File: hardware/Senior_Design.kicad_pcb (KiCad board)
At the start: 4 copper layers, 169 x 146 mm, 155 parts, among them J1 J0011D21BNL, J20 USB_C_Receptacle_USB2.0_16P, J22 Conn_ARM_JTAG_SWD_10, J5 Conn_ARM_JTAG_SWD_10, J6 Barrel_Jack_Switch, Q3 CSD87503Q3E, Q4 CSD87503Q3E, SW1 SW_Push, SW3 SW_Push, U1 USBLC6-2P6, U10 TLV62569ADRL, U2 EFR32FG28A122F1024GM48-A, U20 USBLC6-2P6, U21 USBLC6-2P6, U22 W5500, U23 BDE-MB1352P71UA32, U3 USBLC6-2P6, U33 USBLC6-2P6, U4 TPS61022, U5 BQ25798RQMR, U59 USBLC6-2P6, U6 BME688, U7 USBLC6-2P6, U8 CP2102N-A02-GQFN20, U9 USBLC6-2P6, X1 Crystal_GND2, Y65 25MHz

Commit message: footprint update
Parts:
- added C202: 1uF, Capacitor_SMD:C_0805_2012Metric, F.Cu at (81.9, -146.0)
- added C203: 2.7uF, Capacitor_SMD:C_0805_2012Metric, F.Cu at (81.9, -143.0)
- added C204: 1uF, Capacitor_SMD:C_0805_2012Metric, F.Cu at (81.9, -140.0)
- added C205: 1uF, Capacitor_SMD:C_0805_2012Metric, F.Cu at (81.9, -137.0)
- added C206: 10nF, Capacitor_SMD:C_0805_2012Metric, F.Cu at (81.9, -133.9)
- added C207: 0.1uF, Capacitor_SMD:C_0805_2012Metric, F.Cu at (81.9, -130.9)
- added C208: 0.1uF, Capacitor_SMD:C_0805_2012Metric, F.Cu at (81.9, -127.9)
- added C209: 0.1uF, Capacitor_SMD:C_0805_2012Metric, F.Cu at (81.9, -124.9)
- added C304: 10uF, Capacitor_SMD:C_0805_2012Metric, F.Cu at (60.8, -146.0)
- added C305: 10uF, Capacitor_SMD:C_0805_2012Metric, F.Cu at (60.8, -143.0)
- added C306: 100nF, Capacitor_SMD:C_0805_2012Metric, F.Cu at (60.8, -140.0)
- added C312: 22uF, Capacitor_SMD:C_0805_2012Metric, F.Cu at (60.8, -137.0)
- added C313: 22uF, Capacitor_SMD:C_0805_2012Metric, F.Cu at (60.8, -133.9)
- added C314: 22uF, Capacitor_SMD:C_0805_2012Metric, F.Cu at (60.8, -130.9)
- added C316: 10uF, Capacitor_SMD:C_0805_2012Metric, F.Cu at (60.8, -127.9)
- added C329: 10uF, Capacitor_SMD:C_0805_2012Metric, F.Cu at (60.8, -124.9)
- added D202: LED, LED_SMD:LED_0805_2012Metric, F.Cu at (90.8, -146.0)
- added D203: LED, LED_SMD:LED_0805_2012Metric, F.Cu at (90.8, -142.9)
- added D204: LED, LED_SMD:LED_0805_2012Metric, F.Cu at (90.8, -139.9)
- added D601: LED, LED_SMD:LED_0805_2012Metric, F.Cu at (60.8, -114.9)
- added D602: LED, LED_SMD:LED_0805_2012Metric, F.Cu at (60.8, -111.9)
- added IC301: TLV61220DBVT, pyronet_footprints:SOT95P280X110-6, F.Cu at (75.3, -145.0)
- added J302: Conn_01x03, Connector_JST:JST_PH_S3B-PH-K_1x03_P2.00mm_Horizontal, F.Cu at (66.0, -145.1)
- added L301: 1.5uH, Inductor_SMD:L_0805_2012Metric, F.Cu at (75.1, -136.5)
- added L303: 4.7uH, Inductor_SMD:L_0805_2012Metric, F.Cu at (75.1, -133.7)
- added Q303: Q_NMOS, Package_TO_SOT_SMD:SOT-23_Handsoldering, F.Cu at (71.7, -128.0)
- added R202: 4.7k, Resistor_SMD:R_0805_2012Metric, F.Cu at (86.3, -146.0)
- added R203: 4.7k, Resistor_SMD:R_0805_2012Metric, F.Cu at (86.3, -143.1)
- added R204: 220, Resistor_SMD:R_0805_2012Metric, F.Cu at (86.3, -140.1)
- added R205: 220, Resistor_SMD:R_0805_2012Metric, F.Cu at (86.3, -137.2)
- added R206: 220, Resistor_SMD:R_0805_2012Metric, F.Cu at (86.3, -134.2)
- added R304: 1M, Resistor_SMD:R_0805_2012Metric, F.Cu at (65.2, -136.4)
- added R305: 180k, Resistor_SMD:R_0805_2012Metric, F.Cu at (65.2, -133.4)
- added R308: 1M, Resistor_SMD:R_0805_2012Metric, F.Cu at (65.2, -130.5)
- added R312: 909K, Resistor_SMD:R_0805_2012Metric, F.Cu at (65.2, -127.5)
- added R313: 100K, Resistor_SMD:R_0805_2012Metric, F.Cu at (65.2, -124.6)
- added R402: 10k, Resistor_SMD:R_0805_2012Metric, F.Cu at (71.6, -119.6)
- added R606: 220, Resistor_SMD:R_0805_2012Metric, F.Cu at (65.2, -115.0)
- added R607: 220, Resistor_SMD:R_0805_2012Metric, F.Cu at (65.2, -112.0)
- added U301: TPS63020DSJR, pyronet_footprints:IC_TPS63020DSJR, F.Cu at (70.3, -134.9)
- added U602: CDSOT236-0504C, Package_TO_SOT_SMD:SOT-23-6, F.Cu at (61.1, -118.7)
- added U701: W5500, Package_QFP:LQFP-48_7x7mm_P0.5mm, F.Cu at (85.3, -115.7)
- added Y201: LF_Crystal, Crystal:Crystal_SMD_3215-2Pin_3.2x1.5mm, F.Cu at (86.6, -131.1)
- C201: renamed from C19; footprint Capacitor_SMD:C_0402_1005Metric -> Capacitor_SMD:C_0805_2012Metric
- C301: renamed from C40; footprint Capacitor_SMD:C_0402_1005Metric -> Capacitor_SMD:C_0805_2012Metric
- C302: renamed from C44; footprint Capacitor_SMD:C_0402_1005Metric -> Capacitor_SMD:C_0805_2012Metric
- C303: renamed from C45; footprint Capacitor_SMD:C_0402_1005Metric -> Capacitor_SMD:C_0805_2012Metric
- C307: renamed from C46; footprint Capacitor_SMD:C_0402_1005Metric -> Capacitor_SMD:C_0805_2012Metric
- C308: renamed from C47; footprint Capacitor_SMD:C_0402_1005Metric -> Capacitor_SMD:C_0805_2012Metric
- C309: renamed from C49; footprint Capacitor_SMD:C_0402_1005Metric -> Capacitor_SMD:C_0805_2012Metric
- C310: renamed from C50; footprint Capacitor_SMD:C_0402_1005Metric -> Capacitor_SMD:C_0805_2012Metric
- C311: renamed from C51; footprint Capacitor_SMD:C_0402_1005Metric -> Capacitor_SMD:C_0805_2012Metric
- C315: renamed from C55; footprint Capacitor_SMD:C_0402_1005Metric -> Capacitor_SMD:C_0805_2012Metric
- C317: renamed from C67; footprint Capacitor_SMD:C_0402_1005Metric -> Capacitor_SMD:C_0805_2012Metric
- C318: renamed from C69; footprint Capacitor_SMD:C_0402_1005Metric -> Capacitor_SMD:C_0805_2012Metric
- C319: renamed from C52; footprint Capacitor_SMD:C_0402_1005Metric -> Capacitor_SMD:C_0805_2012Metric
- C320: renamed from C68; footprint Capacitor_SMD:C_0402_1005Metric -> Capacitor_SMD:C_0805_2012Metric
- C321: renamed from C71; footprint Capacitor_SMD:C_0402_1005Metric -> Capacitor_SMD:C_0805_2012Metric
- C322: renamed from C53; footprint Capacitor_SMD:C_0402_1005Metric -> Capacitor_SMD:C_0805_2012Metric
- C323: renamed from C70; footprint Capacitor_SMD:C_0402_1005Metric -> Capacitor_SMD:C_0805_2012Metric
- C324: renamed from C73; footprint Capacitor_SMD:C_0402_1005Metric -> Capacitor_SMD:C_0805_2012Metric
- C325: renamed from C54; footprint Capacitor_SMD:C_0402_1005Metric -> Capacitor_SMD:C_0805_2012Metric
- C326: renamed from C72; footprint Capacitor_SMD:C_0402_1005Metric -> Capacitor_SMD:C_0805_2012Metric
- C327: renamed from C75; footprint Capacitor_SMD:C_0402_1005Metric -> Capacitor_SMD:C_0805_2012Metric
- C328: renamed from C74; footprint Capacitor_SMD:C_0402_1005Metric -> Capacitor_SMD:C_0805_2012Metric
- C401: renamed from C1; footprint Capacitor_SMD:C_0603_1608Metric -> Capacitor_SMD:C_0805_2012Metric
- C402: renamed from C10; footprint Capacitor_SMD:C_0402_1005Metric -> Capacitor_SMD:C_0805_2012Metric
- C403: renamed from C2; footprint Capacitor_SMD:C_0402_1005Metric -> Capacitor_SMD:C_0805_2012Metric
- C501: renamed from C25; footprint Capacitor_SMD:C_0402_1005Metric -> Capacitor_SMD:C_0805_2012Metric
- C502: renamed from C12; footprint Capacitor_SMD:C_0402_1005Metric -> Capacitor_SMD:C_0805_2012Metric
- C601: renamed from C90; footprint Capacitor_SMD:C_0402_1005Metric -> Capacitor_SMD:C_0805_2012Metric
- C602: renamed from C14; footprint Capacitor_SMD:C_0402_1005Metric -> Capacitor_SMD:C_0805_2012Metric
- C701: renamed from C7; footprint Capacitor_SMD:C_0402_1005Metric -> Capacitor_SMD:C_0805_2012Metric
- C702: renamed from C9; footprint Capacitor_SMD:C_0402_1005Metric -> Capacitor_SMD:C_0805_2012Metric
- C703: renamed from C8; footprint Capacitor_SMD:C_0402_1005Metric -> Capacitor_SMD:C_0805_2012Metric
- C704: renamed from C27; footprint Capacitor_SMD:C_0402_1005Metric -> Capacitor_SMD:C_0805_2012Metric
- C705: renamed from C100; footprint Capacitor_SMD:C_0402_1005Metric -> Capacitor_SMD:C_0805_2012Metric
- C706: renamed from C56; footprint Capacitor_SMD:C_0402_1005Metric -> Capacitor_SMD:C_0805_2012Metric
- C707: renamed from C28; footprint Capacitor_SMD:C_0402_1005Metric -> Capacitor_SMD:C_0805_2012Metric
- C708: renamed from C3; footprint Capacitor_SMD:C_0402_1005Metric -> Capacitor_SMD:C_0805_2012Metric
- C709: renamed from C29; footprint Capacitor_SMD:C_0402_1005Metric -> Capacitor_SMD:C_0805_2012Metric
- C710: renamed from C4; footprint Capacitor_SMD:C_0402_1005Metric -> Capacitor_SMD:C_0805_2012Metric
- C711: renamed from C5; footprint Capacitor_SMD:C_0402_1005Metric -> Capacitor_SMD:C_0805_2012Metric
- C712: renamed from C39; footprint Capacitor_SMD:C_0402_1005Metric -> Capacitor_SMD:C_0805_2012Metric
- C713: renamed from C82; footprint Capacitor_SMD:C_0402_1005Metric -> Capacitor_SMD:C_0805_2012Metric
- C714: renamed from C34; footprint Capacitor_SMD:C_0402_1005Metric -> Capacitor_SMD:C_0805_2012Metric
- C715: renamed from C38; footprint Capacitor_SMD:C_0402_1005Metric -> Capacitor_SMD:C_0805_2012Metric
- C716: renamed from C41; footprint Capacitor_SMD:C_0402_1005Metric -> Capacitor_SMD:C_0805_2012Metric
- C717: renamed from C42; footprint Capacitor_SMD:C_0402_1005Metric -> Capacitor_SMD:C_0805_2012Metric
- J201: renamed from J5; footprint Connector_PinHeader_1.27mm:PinHeader_2x05_P1.27mm_Vertical -> Connector_PinHeader_1.27mm:PinHeader_2x05_P1.27mm_Vertical_SMD
- J701: renamed from J1; footprint Custom_Parts:CONN_J0011D21B_PUL -> pyronet_footprints:CONN_J0011D21B_PUL
- L302: renamed from L4; footprint Inductor_SMD:L_7.3x7.3_H3.5 -> Inductor_SMD:L_0805_2012Metric
- Q301: renamed from Q3; footprint Custom_Parts:TRANS_CSD87503Q3E -> pyronet_footprints:TRANS_CSD87503Q3ET
- Q302: renamed from Q4; footprint Custom_Parts:TRANS_CSD87503Q3E -> pyronet_footprints:TRANS_CSD87503Q3ET
- R201: renamed from R2; footprint Resistor_SMD:R_0603_1608Metric -> Resistor_SMD:R_0805_2012Metric
- R301: renamed from R10; footprint Resistor_SMD:R_0603_1608Metric -> Resistor_SMD:R_0805_2012Metric
- R302: renamed from R11; footprint Resistor_SMD:R_0603_1608Metric -> Resistor_SMD:R_0805_2012Metric
- R303: renamed from R34; footprint Resistor_SMD:R_0603_1608Metric -> Resistor_SMD:R_0805_2012Metric
- R306: renamed from R_INT1; footprint Resistor_SMD:R_0603_1608Metric -> Resistor_SMD:R_0805_2012Metric
- R307: renamed from R_QON1; footprint Resistor_SMD:R_0603_1608Metric -> Resistor_SMD:R_0805_2012Metric
- R309: renamed from R38; value 100 -> 4.7K; footprint Resistor_SMD:R_0603_1608Metric -> Resistor_SMD:R_0805_2012Metric
- R310: renamed from R39; footprint Resistor_SMD:R_0603_1608Metric -> Resistor_SMD:R_0805_2012Metric
- R311: renamed from R42; footprint Resistor_SMD:R_0603_1608Metric -> Resistor_SMD:R_0805_2012Metric
- R314: renamed from R_TS1; footprint Resistor_SMD:R_0603_1608Metric -> Resistor_SMD:R_0805_2012Metric
- R315: renamed from R_TS3; footprint Resistor_SMD:R_0603_1608Metric -> Resistor_SMD:R_0805_2012Metric
- R401: renamed from R7; value 10k -> 100k; footprint Resistor_SMD:R_0603_1608Metric -> Resistor_SMD:R_0805_2012Metric
- R601: renamed from R14; footprint Resistor_SMD:R_0603_1608Metric -> Resistor_SMD:R_0805_2012Metric
- R602: renamed from R300; footprint Resistor_SMD:R_0603_1608Metric -> Resistor_SMD:R_0805_2012Metric
- R603: renamed from R9; footprint Resistor_SMD:R_0603_1608Metric -> Resistor_SMD:R_0805_2012Metric
- R604: renamed from R27; footprint Resistor_SMD:R_0603_1608Metric -> Resistor_SMD:R_0805_2012Metric
- R605: renamed from R28; footprint Resistor_SMD:R_0603_1608Metric -> Resistor_SMD:R_0805_2012Metric
- R608: renamed from R26; footprint Resistor_SMD:R_0603_1608Metric -> Resistor_SMD:R_0805_2012Metric
- R701: renamed from R80; footprint Resistor_SMD:R_0603_1608Metric -> Resistor_SMD:R_0805_2012Metric
- R702: renamed from R16; footprint Resistor_SMD:R_0603_1608Metric -> Resistor_SMD:R_0805_2012Metric
- R703: renamed from R12; footprint Resistor_SMD:R_0603_1608Metric -> Resistor_SMD:R_0805_2012Metric
- R704: renamed from R13; footprint Resistor_SMD:R_0603_1608Metric -> Resistor_SMD:R_0805_2012Metric
- R705: renamed from R17; footprint Resistor_SMD:R_0603_1608Metric -> Resistor_SMD:R_0805_2012Metric
- R706: renamed from R18; footprint Resistor_SMD:R_0603_1608Metric -> Resistor_SMD:R_0805_2012Metric
- R707: renamed from R1; footprint Resistor_SMD:R_0603_1608Metric -> Resistor_SMD:R_0805_2012Metric
- R708: renamed from R22; footprint Resistor_SMD:R_0603_1608Metric -> Resistor_SMD:R_0805_2012Metric
- R709: renamed from R23; footprint Resistor_SMD:R_0603_1608Metric -> Resistor_SMD:R_0805_2012Metric
- R710: renamed from R19; footprint Resistor_SMD:R_0603_1608Metric -> Resistor_SMD:R_0805_2012Metric
- R711: renamed from R20; footprint Resistor_SMD:R_0603_1608Metric -> Resistor_SMD:R_0805_2012Metric
- R712: renamed from R21; footprint Resistor_SMD:R_0603_1608Metric -> Resistor_SMD:R_0805_2012Metric
- R713: renamed from R15; footprint Resistor_SMD:R_0603_1608Metric -> Resistor_SMD:R_0805_2012Metric
- R714: renamed from R8; footprint Resistor_SMD:R_0603_1608Metric -> Resistor_SMD:R_0805_2012Metric
- U201: renamed from U2; footprint Custom_Parts:QFN40P600X600X90-49N -> pyronet_footprints:QFN40P600X600X90-49N
- U302: renamed from U5; footprint Custom_Parts:IC_BQ25798RQMR -> pyronet_footprints:IC_BQ25798RQMR
- U403: renamed from U23; footprint Custom_Parts:XCVR_BDE-MB1352P71UA32 -> pyronet_footprints:XCVR_BDE-MB1352P71UA32
- U501: renamed from U6; footprint Custom_Parts:IC_BME688 -> pyronet_footprints:IC_BME688
- U603: renamed from U8; footprint Custom_Parts:QFN50P400X400X80-25N -> pyronet_footprints:SILABS_CP2102N-A02-GQFN20R
- X201: renamed from X1; value Crystal_GND2 -> HF_Crystal; footprint Crystal:Crystal_SMD_3225-4Pin_3.2x2.5mm -> Crystal:Crystal_SMD_2016-4Pin_2.0x1.6mm
- moved D4 0.41 mm to (126.0, 23.4)
- renumbered D9 to D201, D10 to D301, D1 to D302, D2 to D303, D5 to D304, D7 to D401, D11 to D501, FB3 to FB701, J6 to J301, J22 to J401, J20 to J601, SPS30_Connector4 to SPS30_Connector501, SW3 to SW201, SW1 to SW401, U20 to U202, U21 to U203, U1 to U401, U3 to U402, U59 to U502, U33 to U601, U7 to U702, U9 to U703, Y65 to Y701
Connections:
- net /Antenna Module/BDE_RESET renamed /MCU/BDE_RESET
- net /Antenna Module/JTAG_TCKC renamed /Wi-SUN Module/JTAG_TCKC
- net /Antenna Module/JTAG_TDI renamed /Wi-SUN Module/JTAG_TDI
- net /Antenna Module/JTAG_TDO renamed /Wi-SUN Module/JTAG_TDO
- net /Antenna Module/JTAG_TMSC renamed /Wi-SUN Module/JTAG_TMSC
- net /Antenna Module/MCU_CTS_BDE_RTS renamed /MCU/MCU_CTS_BDE_RTS
- net /Antenna Module/MCU_RTS_BDE_CTS renamed /MCU/MCU_RTS_BDE_CTS
- net /Antenna Module/MCU_RX_BDE_TX renamed /MCU/MCU_TX_BDE_RX
- net /Antenna Module/MCU_TX_BDE_RX renamed /MCU/MCU_RX_BDE_TX
- net /MCU/28 renamed /MCU/JTAG_TDO
- net /MCU/INT0 renamed /BMS/INT0
- net /PSU/ACDRV1 renamed /BMS/ACDRV1
- net /PSU/ACDRV2 renamed /BMS/ACDRV2
- net /PSU/PMID renamed /BMS/PMID
- net /PSU/REGN renamed /BMS/REGN
- net /PSU/VAC2 renamed /BMS/VAC2
- net /USBC/D_N renamed /USB-C/D_N
- net /USBC/D_P renamed /USB-C/D_P
- net /ethernet/RD+ renamed /Ethernet/RD+
- net /ethernet/RD- renamed /Ethernet/RD-
- net /ethernet/TD+ renamed /Ethernet/TD+
- net /ethernet/TD- renamed /Ethernet/TD-
- net 5V_VBUS renamed USB_VBUS
- net Net-(J20-CC1) renamed /USB-C/CC1
- net Net-(J20-CC2) renamed /USB-C/CC2
- C315 pad 1: /PSU/SYS -> /BMS/SYS
- C317 pad 1: /PSU/SYS -> /BMS/SYS
- C320 pad 1: /PSU/SYS -> /BMS/SYS
- C323 pad 1: /PSU/SYS -> /BMS/SYS
- C326 pad 1: /PSU/SYS -> /BMS/SYS
- C328 pad 1: /PSU/SYS -> /BMS/SYS
- C402 pad 1: BUCK_3.3V -> +3.3V
- C403 pad 1: BUCK_3.3V -> +3.3V
- C601 pad 1: BUCK_3.3V -> +3.3V
- C602 pad 1: BUCK_3.3V -> +3.3V
- C702 pad 1: BUCK_3.3V -> +3.3V
- C703 pad 1: Net-(U22-XO) -> Net-(U701-XO)
- C704 pad 1: BUCK_3.3V -> +3.3V
- C707 pad 1: Net-(U22-1V2O) -> Net-(U701-1V2O)
- C709 pad 1: Net-(U22-TOCAP) -> Net-(U701-TOCAP)
- D201 pad 1: /MCU/JTAG_RST -> /MCU/nRST
- D501 pad 1: BUCK_5V -> +5V
- FB701 pad 1: BUCK_3.3V -> +3.3V
- J201 pad 1: BUCK_3.3V -> +3.3V
- J201 pad 10: /MCU/JTAG_RST -> /MCU/nRST
- J201 pad 2: /MCU/27 -> /MCU/JTAG_TMS
- J201 pad 4: /MCU/26 -> /MCU/JTAG_TCK
- J201 pad 8: unconnected-(J5-NC/TDI-Pad8) -> /MCU/JTAG_TDI
- J401 pad 1: BUCK_3.3V -> +3.3V
- J701 pad 10: Net-(D3-K) -> Net-(J701-Pad10)
- J701 pad 11: BUCK_3.3V -> +3.3V
- J701 pad 12: Net-(D8-K) -> Net-(J701-Pad12)
- J701 pad 9: BUCK_3.3V -> +3.3V
- R306 pad 2: BUCK_3.3V -> +3.3V
- R307 pad 1: /MCU/QON -> /BMS/QON
- R307 pad 2: BUCK_3.3V -> +3.3V
- R311 pad 1: BAT -> Net-(J302-Pin_1)
- R314 pad 1: /PSU/TS -> /BMS/TS
- R315 pad 2: /PSU/TS -> /BMS/TS
- R401 pad 1: BUCK_3.3V -> +3.3V
- R608 pad 1: Net-(U8-RSTB) -> +3.3V
- R608 pad 2: BUCK_3.3V -> Net-(U603-~{RST})
- R701 pad 1: Net-(U22-XI/CLKIN) -> Net-(U701-XI/CLKIN)
- R702 pad 1: Net-(U22-XI/CLKIN) -> Net-(U701-XI/CLKIN)
- R702 pad 2: Net-(U22-XO) -> Net-(U701-XO)
- R703 pad 1: Net-(U22-TXN) -> Net-(U701-TXN)
- R704 pad 1: Net-(U22-TXP) -> Net-(U701-TXP)
- R705 pad 1: Net-(U22-RXN) -> Net-(U701-RXN)
- R706 pad 1: Net-(U22-RXP) -> Net-(U701-RXP)
- R707 pad 1: Net-(U22-EXRES1) -> Net-(U701-EXRES1)
- R713 pad 1: /ethernet/LINKLED -> /Ethernet/LINKLED
- R713 pad 2: Net-(D3-K) -> Net-(J701-Pad10)
- R714 pad 1: /ethernet/ACTLED -> /Ethernet/ACTLED
- R714 pad 2: Net-(D8-K) -> Net-(J701-Pad12)
- SPS30_Connector501 pad 1: BUCK_5V -> +5V
- SW201 pad 2: Net-(U2-~{RESET}) -> /MCU/nRST
- U201 pad 10: /MCU/INT1 -> /Ethernet/INT1
- U201 pad 13: Net-(U2-~{RESET}) -> /MCU/nRST
- U201 pad 14: BUCK_3.3V -> +3.3V
- U201 pad 15: unconnected-(U2-RFVSS-Pad15) -> GND
- U201 pad 20: /MCU/PAVDD -> +3.3V
- U201 pad 26: /MCU/26 -> /MCU/JTAG_TMS
- U201 pad 27: /MCU/27 -> /MCU/JTAG_TCK
- U201 pad 29: unconnected-(U2-PA04-Pad29) -> /MCU/JTAG_TDI
- U201 pad 33: unconnected-(U2-PA08-Pad33) -> /MCU/SPS30_Debug
- U201 pad 34: unconnected-(U2-PA09-Pad34) -> /MCU/BME688_Degbug
- U201 pad 35: /MCU/JTAG_RST -> /MCU/MCU_Debug
- U201 pad 37: /MCU/VREGSW -> unconnected-(U201-VREGSW-Pad37)
- U201 pad 38: BUCK_3.3V -> +3.3V
- U201 pad 39: unconnected-(U2-VREGVSS-Pad39) -> GND
- U201 pad 40: /MCU/DVDD -> +3.3V
- U201 pad 41: BUCK_3.3V -> +3.3V
- U201 pad 42: BUCK_3.3V -> +3.3V
- U201 pad 43: unconnected-(U2-PD05-Pad43) -> /MCU/BDE_DEBUG1
- U201 pad 44: unconnected-(U2-PD04-Pad44) -> /MCU/BDE_DEBUG0
- U201 pad 45: unconnected-(U2-PD03-Pad45) -> /BMS/QON
- U201 pad 46: /Antenna Module/BDE_DEBUG1 -> unconnected-(U201-PD02-Pad46)
- U201 pad 47: /Antenna Module/BDE_DEBUG0 -> Net-(U201-PD01)
- U201 pad 48: /MCU/QON -> Net-(U201-PD00)
- U201 pad 5: /MCU/SPI_MOSI -> /Ethernet/SPI_MOSI
- U201 pad 6: /MCU/SPI_MISO -> /Ethernet/SPI_MISO
- U201 pad 7: /MCU/SPI_SCK -> /Ethernet/SPI_SCK
- U201 pad 8: /MCU/CS -> /Ethernet/CS
- U202 pad 1: /MCU/26 -> /MCU/JTAG_TCK
- U202 pad 3: /MCU/27 -> /MCU/JTAG_TMS
- U202 pad 4: /MCU/27 -> /MCU/JTAG_TMS
- U202 pad 5: BUCK_3.3V -> +3.3V
- U202 pad 6: /MCU/26 -> /MCU/JTAG_TCK
- U203 pad 3: unconnected-(U21-I/O2-Pad3) -> /MCU/JTAG_TDI
- U203 pad 4: unconnected-(U21-I/O2-Pad4) -> /MCU/JTAG_TDI
- U203 pad 5: BUCK_3.3V -> +3.3V
- U302 pad 12: /MCU/QON -> /BMS/QON
- U302 pad 16: /PSU/TS -> /BMS/TS
- U302 pad 24: unconnected-(U5-SDRV-Pad24) -> Net-(U302-SDRV)
- U302 pad 25: /PSU/SYS -> /BMS/SYS
- U401 pad 5: BUCK_3.3V -> +3.3V
- U402 pad 5: BUCK_3.3V -> +3.3V
- U403 pad 16: /Antenna Module/BDE_DEBUG1 -> /MCU/BDE_DEBUG1
- U403 pad 9: /Antenna Module/BDE_DEBUG0 -> /MCU/BDE_DEBUG0
- U501 pad 2: BUCK_3.3V -> +3.3V
- U501 pad 5: GND -> /BME 688 and SPS30/SCL
- U502 pad 5: BUCK_3.3V -> +3.3V
- U603 pad 10: unconnected-(U8-NC-Pad10) -> (no net)
- U603 pad 19: unconnected-(U8-GPIO.3_/_RXT-Pad19) -> Net-(D602-A)
- U603 pad 20: unconnected-(U8-GPIO.2_/_TXT-Pad20) -> Net-(D601-A)
- U603 pad 6: BUCK_3.3V -> +3.3V
- U603 pad 7: BUCK_3.3V -> +3.3V
- U603 pad 9: Net-(U8-RSTB) -> Net-(U603-~{RST})
- U702 pad 5: BUCK_3.3V -> +3.3V
- U703 pad 5: BUCK_3.3V -> +3.3V
- Y701 pad 3: Net-(U22-XO) -> Net-(U701-XO)
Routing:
- net (no net): track 0.00 -> 696.5 mm, vias 0 -> 18
- net USB_VBUS: track 183.8 -> 0.00 mm, vias 6 -> 0
- net Net-(U2-~{RESET}): track 94.3 -> 1.91 mm, vias 2 -> 0
- net /MCU/nRST: track 60.4 -> 152.8 mm, vias 2 -> 4
- net /MCU/JTAG_RST: track 86.3 -> 0.00 mm, vias 1 -> 0
- net /MCU/26: track 79.3 -> 0.00 mm, vias 2 -> 0
- net /MCU/27: track 78.5 -> 0.00 mm, vias 3 -> 0
- net /Antenna Module/BDE_DEBUG0: track 72.6 -> 0.00 mm, vias 2 -> 0
- net /MCU/QON: track 65.2 -> 0.00 mm, vias 2 -> 0
- net /Antenna Module/BDE_DEBUG1: track 57.5 -> 0.00 mm, vias 2 -> 0
- net Net-(C712-Pad1): track 27.2 -> 0.00 mm
- net /Ethernet/TD+: track 24.4 -> 5.22 mm
- net Net-(C714-Pad1): track 9.89 -> 0.00 mm
- net Net-(U603-VBUS): track 5.75 -> 0.00 mm
- net /MCU/JTAG_TMS: track 0.00 -> 4.99 mm, vias 0 -> 1
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- added copper zone on In2.Cu, net +3.3V
- removed copper zone on In2.Cu, net BUCK_3.3V

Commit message: footprint update 2
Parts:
- removed D12, D3, D4, D6, D8: CSD01060A, Package_TO_SOT_THT:TO-220-2_Vertical
- removed J_BAT1: Conn_01x02, Connector_PinHeader_1.27mm:PinHeader_1x02_P1.27mm_Vertical
- removed L2, L7: 1 uH, Inductor_SMD:L_7.3x7.3_H3.5
- removed R40: 453K, Resistor_SMD:R_0603_1608Metric
- removed R41: 100k, Resistor_SMD:R_0603_1608Metric
- removed U10: TLV62569ADRL, Package_TO_SOT_SMD:SOT-563
- removed the U701 at (85.3, -115.7)
- D201, D301, D401, D501: footprint Package_TO_SOT_THT:TO-220-2_Vertical -> Diode_SMD:D_SOD-123
- moved C202 257.9 mm to (-65.3, 65.8)
- moved C203 257.9 mm to (-65.3, 68.8)
- moved C204 257.9 mm to (-65.3, 71.8)
- moved C205 257.9 mm to (-65.3, 74.8)
- moved C206 257.9 mm to (-65.3, 77.8)
- moved C207 257.9 mm to (-65.3, 80.8)
- moved C208 257.9 mm to (-65.3, 83.8)
- moved C209 257.9 mm to (-65.3, 86.8)
- moved C304 257.9 mm to (-86.4, 65.8)
- moved C305 257.9 mm to (-86.4, 68.8)
- moved C306 257.9 mm to (-86.4, 71.8)
- moved C312 257.9 mm to (-86.4, 74.8)
- moved C313 257.9 mm to (-86.4, 77.8)
- moved C314 257.9 mm to (-86.4, 80.8)
- moved C316 257.9 mm to (-86.4, 83.8)
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- renumbered U22 to U701
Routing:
- net /MCU/MCU_Debug: track 0.00 -> 86.3 mm
- net (no net): track 696.5 -> 610.2 mm
- net Net-(J701-Pad12): track 0.00 -> 14.6 mm
- net Net-(D8-K): track 14.6 -> 0.00 mm
- net /MCU/BDE_RESET: track 42.1 -> 32.5 mm
- net Net-(J701-Pad10): track 0.00 -> 5.15 mm
- net Net-(D3-K): track 5.15 -> 0.00 mm

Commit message: layout_246
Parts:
- moved C306 231.4 mm to (129.1, 156.0)
- moved C305 230.0 mm to (128.6, 150.4)
- moved C312 220.5 mm to (122.0, 146.8)
- moved C304 219.5 mm to (120.0, 140.7)
- moved U602 218.6 mm to (123.4, 30.5)
- moved J302 218.5 mm to (130.6, 120.4)
- moved U301 214.1 mm to (128.5, 137.1)
- moved L301 212.8 mm to (129.0, 144.8), turned to 180 degrees
- moved C316 206.8 mm to (106.2, 159.0)
- moved R304 206.4 mm to (108.7, 154.4)
- moved IC301 205.7 mm to (123.2, 132.1)
- moved C313 204.5 mm to (106.2, 146.3)
- moved C314 202.0 mm to (106.2, 141.7)
- moved R305 198.5 mm to (100.7, 156.0)
- moved R313 198.1 mm to (109.8, 136.7)
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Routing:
- net (no net): track 610.2 -> 417.2 mm, vias 18 -> 12
- net USB_VBUS: track 0.00 -> 154.2 mm, vias 0 -> 3
- net /MCU/SPI_MOSI: track 36.9 -> 14.1 mm
- net /Ethernet/SPI_MOSI: track 0.00 -> 22.8 mm
- net /MCU/SPI_MISO: track 35.1 -> 12.9 mm
- net /Ethernet/SPI_MISO: track 0.00 -> 22.2 mm
- net /Ethernet/SPI_SCK: track 0.00 -> 19.0 mm
- net /MCU/SPI_SCK: track 33.5 -> 14.5 mm
- net /Ethernet/CS: track 0.00 -> 18.3 mm
- net /MCU/CS: track 32.0 -> 13.7 mm
- net /MCU/INT1: track 40.5 -> 22.4 mm, vias 4 -> 3
- net /Ethernet/INT1: track 0.00 -> 18.1 mm, vias 0 -> 1
- net /USB-C/D_P: track 12.7 -> 1.54 mm, vias 2 -> 0
- net /USB-C/D_N: track 12.0 -> 2.87 mm
- net Net-(U22-XO): track 14.2 -> 6.94 mm
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
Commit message: pcb_update_1232
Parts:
- removed C16: 10uF, Capacitor_SMD:C_0402_1005Metric
- removed C20: 10nF, Capacitor_SMD:C_0402_1005Metric
- removed C21, C36: 100nF, Capacitor_SMD:C_0402_1005Metric
- removed C23, C33, C37: 1uF, Capacitor_SMD:C_0402_1005Metric
- removed C24, C31, C32: 0.1uF, Capacitor_SMD:C_0402_1005Metric
- removed C35: 120pF, Capacitor_SMD:C_0402_1005Metric
- removed C87: 4.7uF, Capacitor_SMD:C_0402_1005Metric
- removed FB1: BLM03AG700SN1, Resistor_SMD:R_0201_0603Metric
- removed FB2: BLM03PG330SN1, Resistor_SMD:R_0603_1608Metric
- removed L3: 2.2uH, Inductor_SMD:L_7.3x7.3_H3.5
- removed R3, R4, R5, R6: 4.7k, Resistor_SMD:R_0603_1608Metric
- removed U601: USBLC6-2P6, Package_TO_SOT_SMD:SOT-666
- added D305: SMAJ12A, Diode_SMD:D_SMA, F.Cu at (81.3, 129.4)
- added D603: SMAJ12A, Diode_SMD:D_SMA, F.Cu at (96.2, 23.8)
- added R715: 0, Resistor_SMD:R_0805_2012Metric, F.Cu at (143.5, 49.5)
- added REF**: MountingHole_2.1mm, MountingHole:MountingHole_2.1mm, F.Cu at (158.5, 26.0)
- added REF**: MountingHole_2.1mm, MountingHole:MountingHole_2.1mm, F.Cu at (152.7, 163.3)
- added REF**: MountingHole_2.1mm, MountingHole:MountingHole_2.1mm, F.Cu at (26.7, 24.1)
- added REF**: MountingHole_2.1mm, MountingHole:MountingHole_2.1mm, F.Cu at (26.7, 162.6)
- L301: footprint Inductor_SMD:L_0805_2012Metric -> Inductor_SMD:L_Wuerth_MAPI-4020
- L302: footprint Inductor_SMD:L_0805_2012Metric -> Inductor_SMD:L_Bourns_SRP7028A_7.3x6.6mm
- L303: footprint Inductor_SMD:L_0805_2012Metric -> Inductor_SMD:L_1210_3225Metric
- moved C501 174.5 mm to (24.1, 138.1), turned to 90 degrees
- moved C502 167.8 mm to (27.8, 138.0), turned to -90 degrees
- moved U501 166.6 mm to (25.2, 131.9), turned to 90 degrees
- moved SPS30_Connector501 153.5 mm to (25.3, 98.2), turned to 0 degrees
- moved D501 153.3 mm to (30.1, 98.1), turned to 0 degrees
- moved U502 145.4 mm to (31.3, 102.7), turned to 90 degrees
- moved D202 59.3 mm to (89.1, 73.0)
- moved D203 58.1 mm to (89.0, 69.5)
- moved D204 55.6 mm to (89.2, 76.4)
- moved IC301 53.0 mm to (71.5, 143.8)
- moved U301 49.9 mm to (81.0, 152.2)
- moved R205 47.0 mm to (79.7, 65.3)
- moved R204 46.6 mm to (79.8, 68.7), turned to 180 degrees
- moved C312 46.3 mm to (75.7, 147.7)
- moved C601 44.9 mm to (77.3, 39.0), turned to -90 degrees
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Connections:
- FB701 pad 2: +3.3VA -> Net-(FB701-Pad2)
- SPS30_Connector501 pad 2: /BME 688 and SPS30/SDA -> Net-(SPS30_Connector501-Pin_2)
- SPS30_Connector501 pad 3: /BME 688 and SPS30/SCL -> Net-(SPS30_Connector501-Pin_3)
- U502 pad 4: /BME 688 and SPS30/SCL -> Net-(SPS30_Connector501-Pin_3)
- U502 pad 6: /BME 688 and SPS30/SDA -> Net-(SPS30_Connector501-Pin_2)
- U602 pad 5: USB_VBUS -> +3.3V
- U701 pad 1: Net-(U22-TXN) -> Net-(U701-TXN)
- U701 pad 10: Net-(U22-EXRES1) -> Net-(U701-EXRES1)
- U701 pad 2: Net-(U22-TXP) -> Net-(U701-TXP)
- U701 pad 20: Net-(U22-TOCAP) -> Net-(U701-TOCAP)
- U701 pad 22: Net-(U22-1V2O) -> Net-(U701-1V2O)
- U701 pad 25: /ethernet/LINKLED -> /Ethernet/LINKLED
- U701 pad 27: /ethernet/ACTLED -> /Ethernet/ACTLED
- U701 pad 28: BUCK_3.3V -> +3.3V
- U701 pad 30: Net-(U22-XI/CLKIN) -> Net-(U701-XI/CLKIN)
- U701 pad 31: Net-(U22-XO) -> Net-(U701-XO)
- U701 pad 32: /MCU/CS -> /Ethernet/CS
- U701 pad 33: /MCU/SPI_SCK -> /Ethernet/SPI_SCK
- U701 pad 34: /MCU/SPI_MISO -> /Ethernet/SPI_MISO
- U701 pad 35: /MCU/SPI_MOSI -> /Ethernet/SPI_MOSI
- U701 pad 36: /MCU/INT1 -> /Ethernet/INT1
- U701 pad 43: BUCK_3.3V -> +3.3V
- U701 pad 44: BUCK_3.3V -> +3.3V
- U701 pad 45: BUCK_3.3V -> +3.3V
- U701 pad 5: Net-(U22-RXN) -> Net-(U701-RXN)
- U701 pad 6: Net-(U22-RXP) -> Net-(U701-RXP)
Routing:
- net (no net): track 417.2 -> 98.4 mm, vias 12 -> 2
- net BUCK_5V: track 177.2 -> 7.31 mm
- net USB_VBUS: track 154.2 -> 72.5 mm, vias 3 -> 4
- net /BME 688 and SPS30/SCL: track 133.4 -> 209.4 mm
- net /MCU/MCU_Debug: track 86.3 -> 15.0 mm
- net /BME 688 and SPS30/SDA: track 137.2 -> 208.4 mm
- net /ethernet/LINKLED: track 57.0 -> 0.00 mm, vias 2 -> 0
- net /Ethernet/LINKLED: track 0.00 -> 54.4 mm, vias 0 -> 2
- net Net-(U201-PD00): track 0.00 -> 53.0 mm, vias 0 -> 1
- net /MCU/BDE_RESET: track 32.5 -> 83.9 mm, vias 0 -> 1
- net /MCU/MCU_RX_BDE_TX: track 50.9 -> 0.00 mm
- net /ethernet/ACTLED: track 49.8 -> 0.00 mm, vias 2 -> 0
- net /Ethernet/ACTLED: track 0.00 -> 48.3 mm, vias 0 -> 2
- net /MCU/DVDD: track 41.0 -> 0.00 mm
- net /MCU/JTAG_TDO: track 77.8 -> 37.1 mm, vias 2 -> 1
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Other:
- board size 169 x 146 mm -> 144 x 146 mm

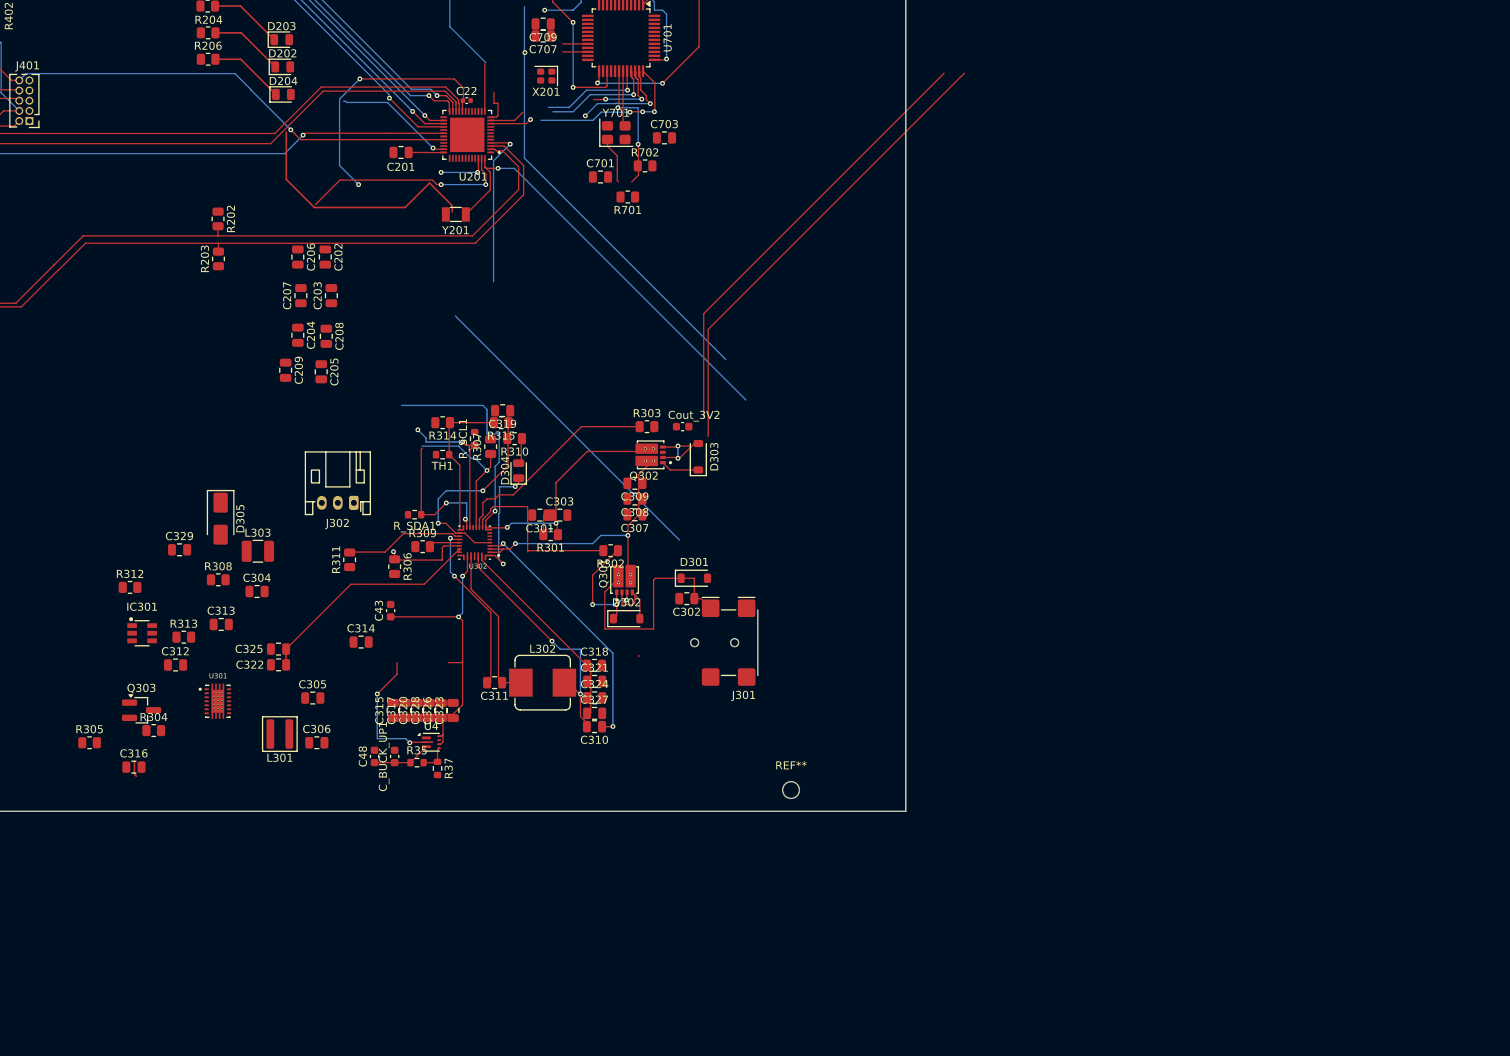
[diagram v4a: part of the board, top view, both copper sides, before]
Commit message: Buck/Bost layouts and part of BMS
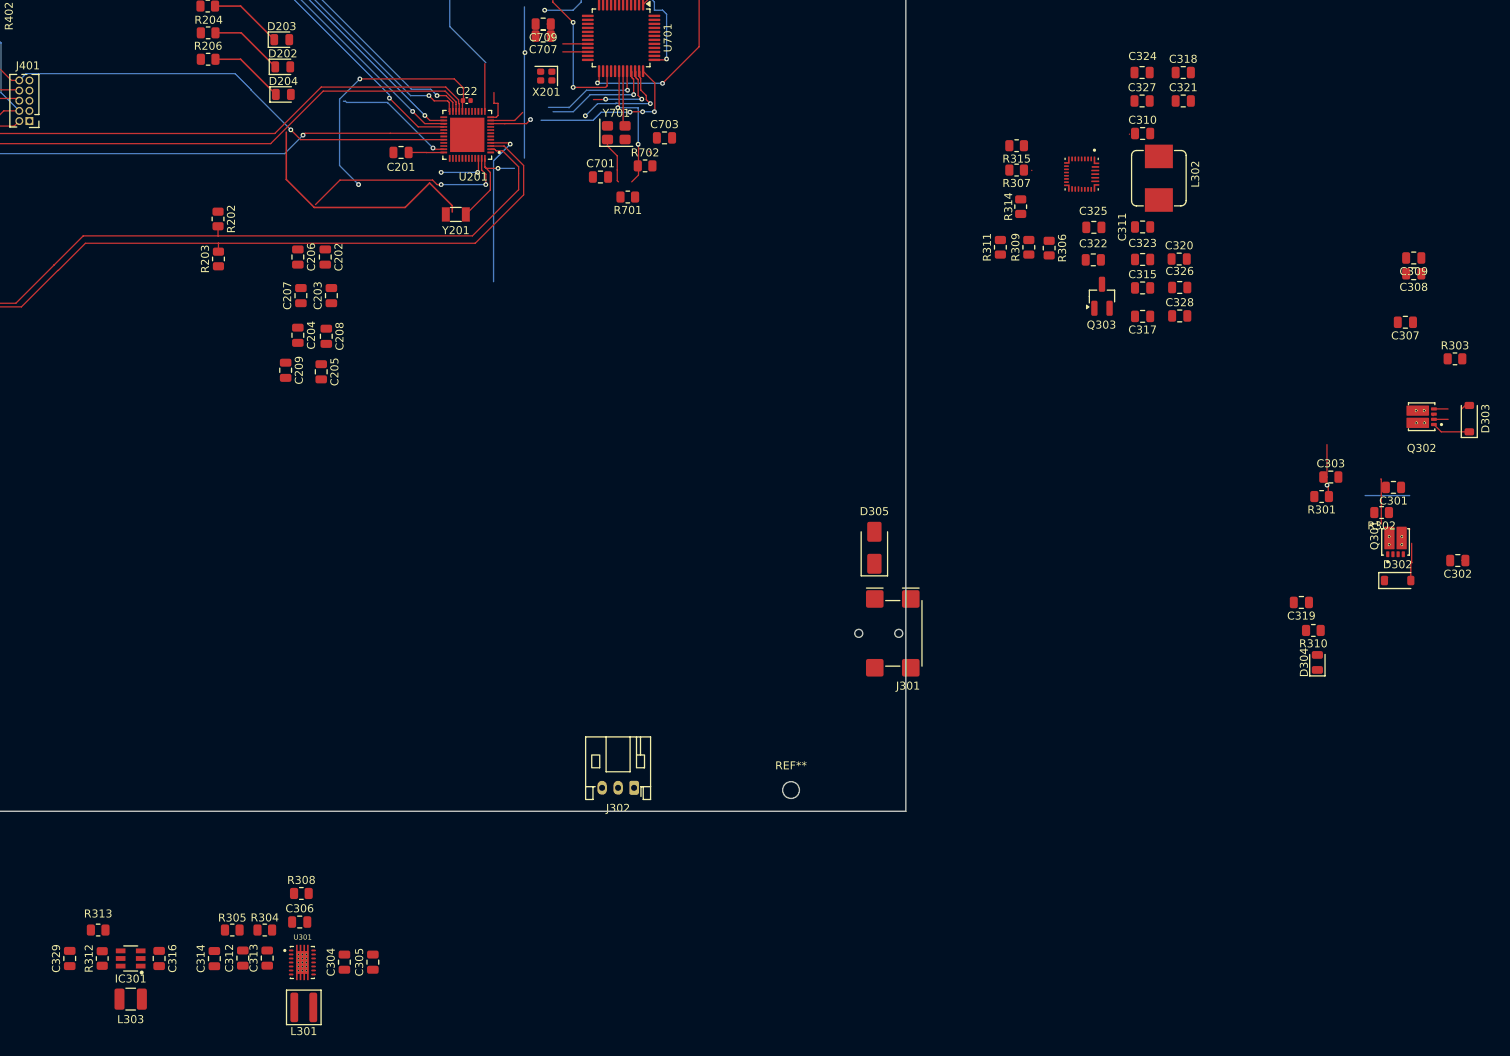
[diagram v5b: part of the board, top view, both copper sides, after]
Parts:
- removed C43: 10uF, Capacitor_SMD:C_0603_1608Metric
- removed C48, Cout_3V2: 22uF, Capacitor_SMD:C_0603_1608Metric
- removed C_BUCK_UP1: 4.7uF, Capacitor_SMD:C_0603_1608Metric
- removed D301: CSD01060A, Diode_SMD:D_SOD-123
- removed R35: 910k, Resistor_SMD:R_0603_1608Metric
- removed R37: 100k, Resistor_SMD:R_0603_1608Metric
- removed R_SCL1, R_SDA1: 4.7K, Resistor_SMD:R_0603_1608Metric
- removed TH1: NTC 10k, Resistor_SMD:R_0603_1608Metric
- removed U4: TPS61022, Package_DFN_QFN:Texas_RWU0007A_VQFN-7_2x2mm_P0.5mm
- moved Q303 130.7 mm to (191.5, 101.6), turned to 90 degrees
- moved C325 114.7 mm to (190.5, 93.0)
- moved C322 113.7 mm to (190.4, 97.1)
- moved C320 110.7 mm to (201.2, 97.0), turned to 0 degrees
- moved C315 107.6 mm to (196.6, 100.6), turned to 0 degrees
- moved C301 106.8 mm to (228.0, 125.5)
- moved C326 106.4 mm to (201.2, 100.5), turned to 0 degrees
- moved C328 106.0 mm to (201.2, 104.1), turned to 0 degrees
- moved C317 104.5 mm to (196.6, 104.1), turned to 180 degrees
- moved C318 104.4 mm to (201.7, 73.7)
- moved C324 103.9 mm to (196.5, 73.7), turned to 180 degrees
- moved C321 103.3 mm to (201.7, 77.2)
- moved C323 103.0 mm to (196.6, 97.0), turned to 0 degrees
- moved C319 102.7 mm to (216.4, 139.9)
- moved D304 102.7 mm to (218.4, 147.4)
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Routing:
- net /BME 688 and SPS30/SDA: track 208.4 -> 131.9 mm, vias 2 -> 0
- net /BME 688 and SPS30/SCL: track 209.4 -> 135.1 mm, vias 2 -> 0
- net /BMS/INT0: track 71.0 -> 20.6 mm, vias 2 -> 1
- net USB_VBUS: track 72.5 -> 27.7 mm, vias 4 -> 2
- net /PSU/SYS: track 43.9 -> 0.00 mm, vias 2 -> 0
- net Net-(U201-PD00): track 53.0 -> 12.1 mm
- net Net-(C307-Pad1): track 35.7 -> 0.00 mm, vias 2 -> 0
- net /MCU/nRST: track 116.1 -> 80.5 mm
- net Net-(U302-BTST1): track 32.2 -> 0.03 mm, vias 2 -> 0
- net Net-(U302-SW1): track 30.7 -> 0.00 mm, vias 2 -> 0
- net BAT: track 29.2 -> 0.00 mm
- net /BMS/VAC2: track 29.8 -> 0.65 mm
- net /BMS/REGN: track 27.9 -> 0.04 mm, vias 2 -> 0
- net /BMS/ACDRV1: track 26.9 -> 0.00 mm
- net /BMS/PMID: track 25.5 -> 0.00 mm
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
